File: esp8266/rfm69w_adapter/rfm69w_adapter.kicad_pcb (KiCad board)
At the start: 2 copper layers, 20 x 17.8 mm, 62 parts, among them J1 Conn_01x01, J10 Conn_01x01, J11 Conn_01x01, J12 Conn_01x01, J13 Conn_01x01, J14 Conn_01x01, J15 Conn_01x01, J16 Conn_01x01, J2 Conn_01x01, J3 Conn_01x01, J4 Conn_01x01, J5 Conn_01x01, J6 Conn_01x01, J7 Conn_01x01, J8 Conn_01x01, J9 Conn_01x01, U1 ESP8266EX, U2 AT25SF321-SSHDB, Y1 26MHz

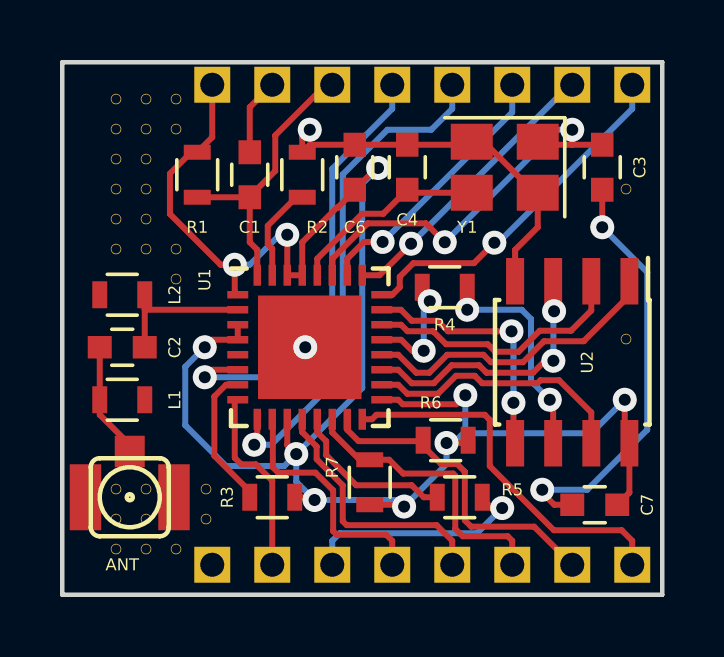
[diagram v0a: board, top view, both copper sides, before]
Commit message: esp8266 to rfm69 adapter refactorings
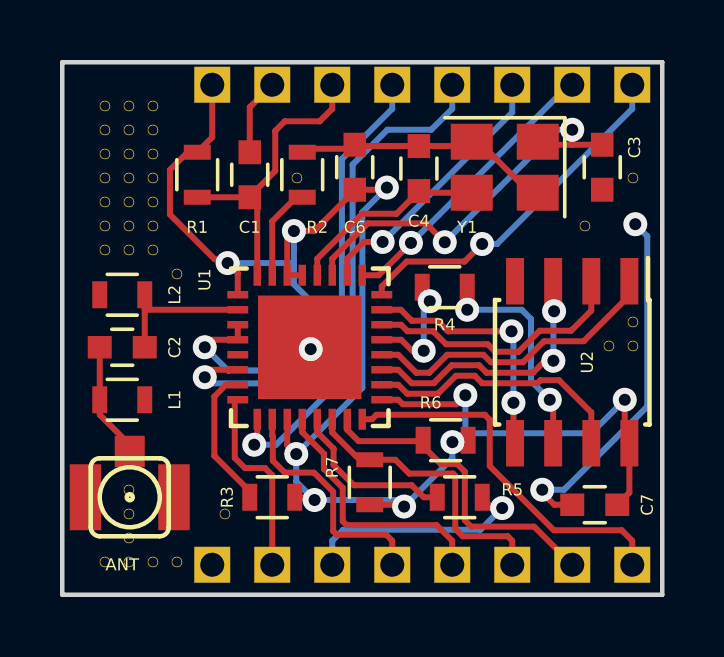
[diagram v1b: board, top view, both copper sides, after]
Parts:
- removed V19_11, V19_6, V2_16, V2_17, V2_18, V2_3, V3_16, V3_17, V3_18, V3_3, V4_18, V4_3, V5_16, V5_17: AUTO_VIA, VIA_MATRIX
- added V10_7: AUTO_VIA, VIA_MATRIX, F.Cu at (120.6, 66.6)
- added V22_9: AUTO_VIA, VIA_MATRIX, F.Cu at (130.2, 68.2)
- added V23_14: AUTO_VIA, VIA_MATRIX, F.Cu at (131.0, 72.2)
- added V24_13: AUTO_VIA, VIA_MATRIX, F.Cu at (131.8, 71.4)
- added V24_14: AUTO_VIA, VIA_MATRIX, F.Cu at (131.8, 72.2)
- added V24_7: AUTO_VIA, VIA_MATRIX, F.Cu at (131.8, 66.6)
- added V2_10: AUTO_VIA, VIA_MATRIX, F.Cu at (114.2, 69.0)
- added V2_23: AUTO_VIA, VIA_MATRIX, F.Cu at (114.2, 79.4)
- added V2_9: AUTO_VIA, VIA_MATRIX, F.Cu at (114.2, 68.2)
- added V3_10: AUTO_VIA, VIA_MATRIX, F.Cu at (115.0, 69.0)
- added V3_20: AUTO_VIA, VIA_MATRIX, F.Cu at (115.0, 77.0)
- added V3_21: AUTO_VIA, VIA_MATRIX, F.Cu at (115.0, 77.8)
- added V3_22: AUTO_VIA, VIA_MATRIX, F.Cu at (115.0, 78.6)
- added V3_23: AUTO_VIA, VIA_MATRIX, F.Cu at (115.0, 79.4)
- added V3_9: AUTO_VIA, VIA_MATRIX, F.Cu at (115.0, 68.2)
- added V4_10: AUTO_VIA, VIA_MATRIX, F.Cu at (115.8, 69.0)
- added V4_23: AUTO_VIA, VIA_MATRIX, F.Cu at (115.8, 79.4)
- added V4_5: AUTO_VIA, VIA_MATRIX, F.Cu at (115.8, 65.0)
- added V4_6: AUTO_VIA, VIA_MATRIX, F.Cu at (115.8, 65.8)
- added V4_7: AUTO_VIA, VIA_MATRIX, F.Cu at (115.8, 66.6)
- added V5_11: AUTO_VIA, VIA_MATRIX, F.Cu at (116.6, 69.8)
- added V5_23: AUTO_VIA, VIA_MATRIX, F.Cu at (116.6, 79.4)
- added V7_21: AUTO_VIA, VIA_MATRIX, F.Cu at (118.2, 77.8)
- moved V4_9 1.93 mm to (115.8, 68.2)
- moved V4_8 1.75 mm to (115.8, 67.4)
- moved V3_8 1.67 mm to (115.0, 67.4)
- moved V2_8 1.61 mm to (114.2, 67.4)
- moved V3_7 1.48 mm to (115.0, 66.6)
- moved V2_7 1.42 mm to (114.2, 66.6)
- moved V3_6 1.30 mm to (115.0, 65.8)
- moved V2_6 1.23 mm to (114.2, 65.8)
- moved V3_5 1.13 mm to (115.0, 65.0)
- moved V4_4 1.09 mm to (115.8, 64.2)
- moved V2_5 1.04 mm to (114.2, 65.0)
- moved V3_4 0.96 mm to (115.0, 64.2)
- moved V2_4 0.85 mm to (114.2, 64.2)
- moved C4 0.39 mm to (124.6, 66.3)
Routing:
- net GND: track 37.1 -> 31.6 mm, vias 5 -> 4
- net +3V3: track 63.6 -> 64.8 mm
- net /RESET: track 9.47 -> 10.1 mm

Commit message: esp8266 rfm69w adapter refactorings
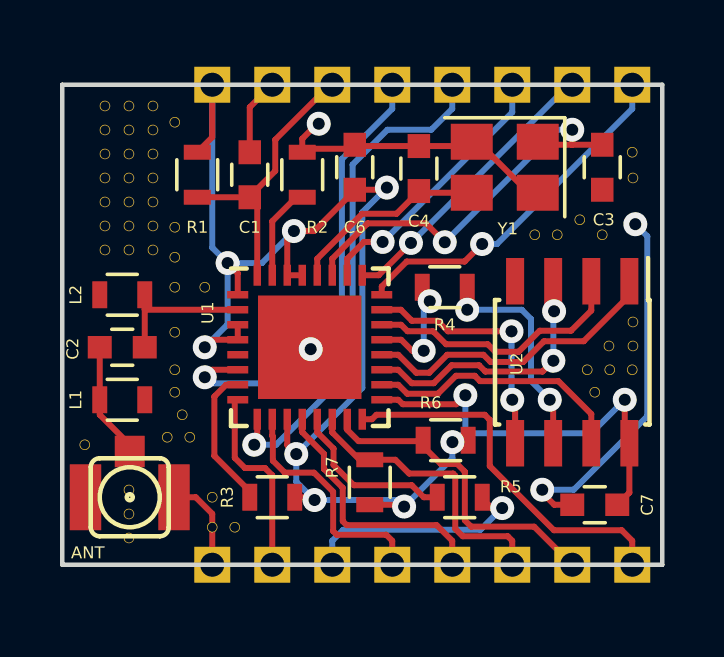
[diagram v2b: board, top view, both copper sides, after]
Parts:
- removed V10_7, V2_23, V3_23, V4_23, V5_23: AUTO_VIA, VIA_MATRIX
- removed the V5_11 at (116.6, 69.8)
- removed the V7_21 at (118.2, 77.8)
- added V22_9: AUTO_VIA, VIA_MATRIX, F.Cu at (131.8, 65.8)
- added V22_9: AUTO_VIA, VIA_MATRIX, F.Cu at (130.8, 68.5)
- added V22_9: AUTO_VIA, VIA_MATRIX, F.Cu at (129.2, 68.5)
- added V22_9: AUTO_VIA, VIA_MATRIX, F.Cu at (128.5, 68.5)
- added V23_14: AUTO_VIA, VIA_MATRIX, F.Cu at (130.5, 73.8)
- added V23_14: AUTO_VIA, VIA_MATRIX, F.Cu at (131.8, 73.0)
- added V23_14: AUTO_VIA, VIA_MATRIX, F.Cu at (131.0, 73.0)
- added V23_14: AUTO_VIA, VIA_MATRIX, F.Cu at (130.2, 73.0)
- added V4_5: AUTO_VIA, VIA_MATRIX, F.Cu at (116.5, 64.8)
- added V4_9: AUTO_VIA, VIA_MATRIX, F.Cu at (116.5, 68.2)
- added V5_11: AUTO_VIA, VIA_MATRIX, F.Cu at (116.5, 69.2)
- added V5_11: AUTO_VIA, VIA_MATRIX, F.Cu at (116.5, 70.2)
- added V5_11: AUTO_VIA, VIA_MATRIX, F.Cu at (117.5, 70.2)
- added V7_21: AUTO_VIA, VIA_MATRIX, F.Cu at (116.5, 71.8)
- added V7_21: AUTO_VIA, VIA_MATRIX, F.Cu at (117.8, 77.2)
- added V7_21: AUTO_VIA, VIA_MATRIX, F.Cu at (116.5, 73.0)
- added V7_21: AUTO_VIA, VIA_MATRIX, F.Cu at (113.5, 75.5)
- added V7_21: AUTO_VIA, VIA_MATRIX, F.Cu at (116.5, 73.8)
- added V7_21: AUTO_VIA, VIA_MATRIX, F.Cu at (117.0, 75.2)
- added V7_21: AUTO_VIA, VIA_MATRIX, F.Cu at (116.8, 74.5)
- added V7_21: AUTO_VIA, VIA_MATRIX, F.Cu at (116.2, 75.2)
- added V7_21: AUTO_VIA, VIA_MATRIX, F.Cu at (118.5, 78.2)
- added V7_21: AUTO_VIA, VIA_MATRIX, F.Cu at (117.8, 78.2)
- moved V22_9 0.27 mm to (130.0, 68.0)
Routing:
- net +3V3: track 64.8 -> 59.6 mm
- net GND: track 31.6 -> 36.0 mm, vias 4 -> 5
- net /RESET: track 10.1 -> 9.42 mm
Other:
- board size 20 x 17.8 mm -> 20 x 16 mm
